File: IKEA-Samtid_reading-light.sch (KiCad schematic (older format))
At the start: 19 parts, among them P1 CONN_2, U1 PT4115-SOT89-5

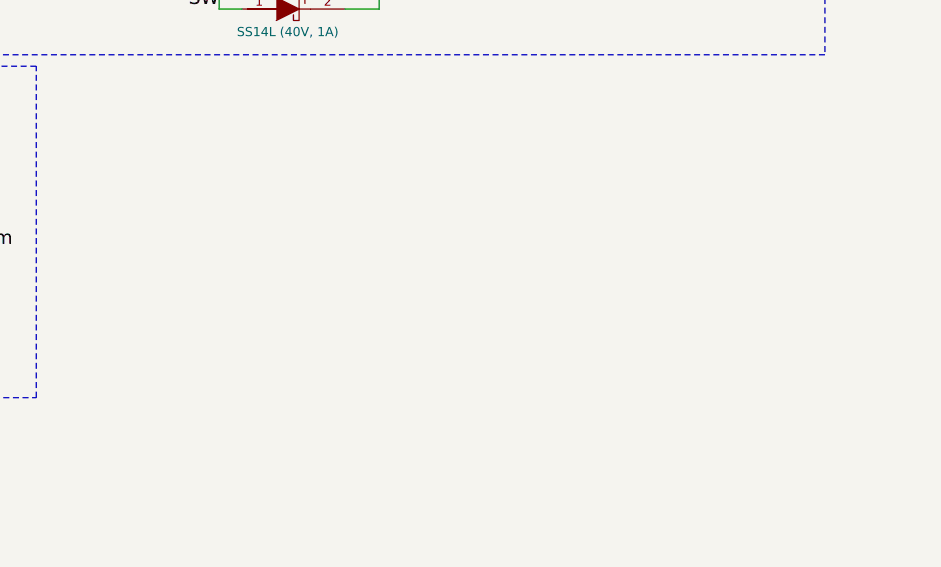
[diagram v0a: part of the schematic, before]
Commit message: Chose ATtiny25 for high-speed PWM (PLL).
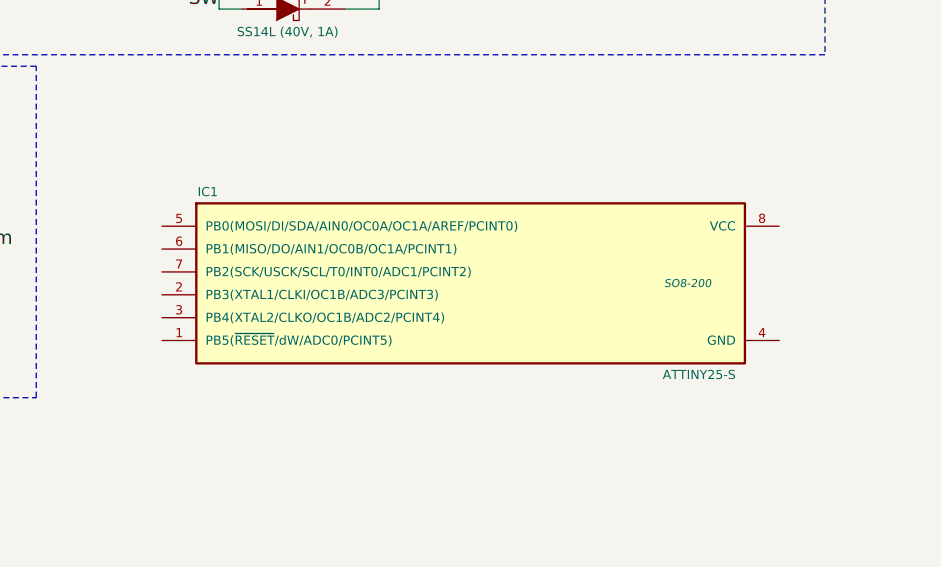
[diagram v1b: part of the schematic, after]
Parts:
- added IC1: ATTINY25-S, SO8-200, symbol ATTINY25-S
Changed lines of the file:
@@
 EESchema Schematic File Version 2
 LIBS:my_parts
+LIBS:atmel
 LIBS:power
 LIBS:device
@@
 LIBS:siliconi
 LIBS:opto
-LIBS:atmel
 LIBS:contrib
 LIBS:valves
@@
 Wire Wire Line
 	5900 2200 6000 2200
+$Comp
+L ATTINY25-S IC1
+U 1 1 5384DAB7
+P 3350 3100
+F 0 "IC1" H 2200 3500 40  0000 C CNN
+F 1 "ATTINY25-S" H 4350 2700 40  0000 C CNN
+F 2 "SO8-200" H 4300 3100 35  0000 C CIN
+F 3 "" H 3350 3100 60  0000 C CNN
+	1    3350 3100
+	1    0    0    -1
+$EndComp
 $EndSCHEMATC

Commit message: Shoving parts around.
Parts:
- removed C4: 10µF, symbol C
- removed P1: CONN_2, symbol CONN_2
- added C1: 10µF, symbol C
- added FSEN1, FSEN2: CONN_2, symbol CONN_2
- added JP1: AVR_ISP, symbol MADW__AVR_ISP
- added P1: CONN_4, symbol CONN_4
- added R_FS1, R_FS2: 1M, symbol R
- added U1: MCP1804-SOT23-5, symbol MADW__MCP1804-SOT23-5
- C2: value 10µF -> 100nF
- C4: renamed from C5; value 10µF -> 100nF
- C5: renamed from C1; value 10µF -> 100nF
- renumbered U1 to U2
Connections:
- net DIM: now also IC1.3 (PB4(XTAL2/CLKO/OC1B/ADC2/PCINT4))
- net GND: now also IC1.4 (GND), C1.2, FSEN2.2 (PM), JP1.6 (GND), P1.3 (P3), P1.4 (P4), R_FS2.2, U1.2 (GND)
- net RESET: now reaches IC1.1 (PB5(~RESET~/dW/ADC0/PCINT5))
- net RESET: now also JP1.5 (RST)
- net FSEN: now reaches IC1.2 (PB3(XTAL1/CLKI/OC1B/ADC3/PCINT3))
- net FSEN: now also FSEN1.2 (PM), FSEN2.1 (P1), R_FS1.2, R_FS2.1
- net MOSI: now reaches IC1.5 (PB0(MOSI/DI/SDA/AIN0/OC0A/OC1A/AREF/PCINT0))
- net MOSI: now also JP1.4 (MOSI)
- net MISO: now reaches IC1.6 (PB1(MISO/DO/AIN1/OC0B/OC1A/PCINT1))
- net MISO: now also JP1.1 (MISO)
- net SCK: now reaches IC1.7 (PB2(SCK/USCK/SCL/T0/INT0/ADC1/PCINT2))
- net SCK: now also JP1.3 (SCK)
- net +5V: now reaches IC1.8 (VCC)
- net +5V: now also C3.1, C4.1, FSEN1.1 (P1), JP1.2 (VTG), R_FS1.1, U1.5 (OUT)
- net D1HS: no longer names the net of D1.2 (K), D2.1 (A)
- net D2HS: no longer names the net of D2.2 (K), D3.1 (A)
- net D3HS: no longer names the net of D3.2 (K), D4.1 (A)
- net D4HS: no longer names the net of D4.2 (K), D5.1 (A)
- net D5HS: no longer names the net of D5.2 (K), D6.1 (A)
- net D6HS: no longer names the net of D6.2 (K), L1.2
- net VCC renamed +24V
- net +24V: now also C1.1, P1.1 (P1), P1.2 (P2), U1.1 (Vin), U1.4 (SHDN); no longer C3.1, C4.1
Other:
- note added: "5V power supply"
- note added: "Analog finger sensor"
- note added: "Brainz"
- note added: "LED driver + LEDs"
- note added: "PT4115 input protection"
- note removed: "(*) Don't use C6 when driving DIM with a 5V PWM signal.\n Replace R1 with a 10k pull-down resistor."
- note removed: "(24V)"
- moved on the sheet: C2, C4, C5, D1, D2, D3, D4, D5, D6, DS1, DZ1, IC1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

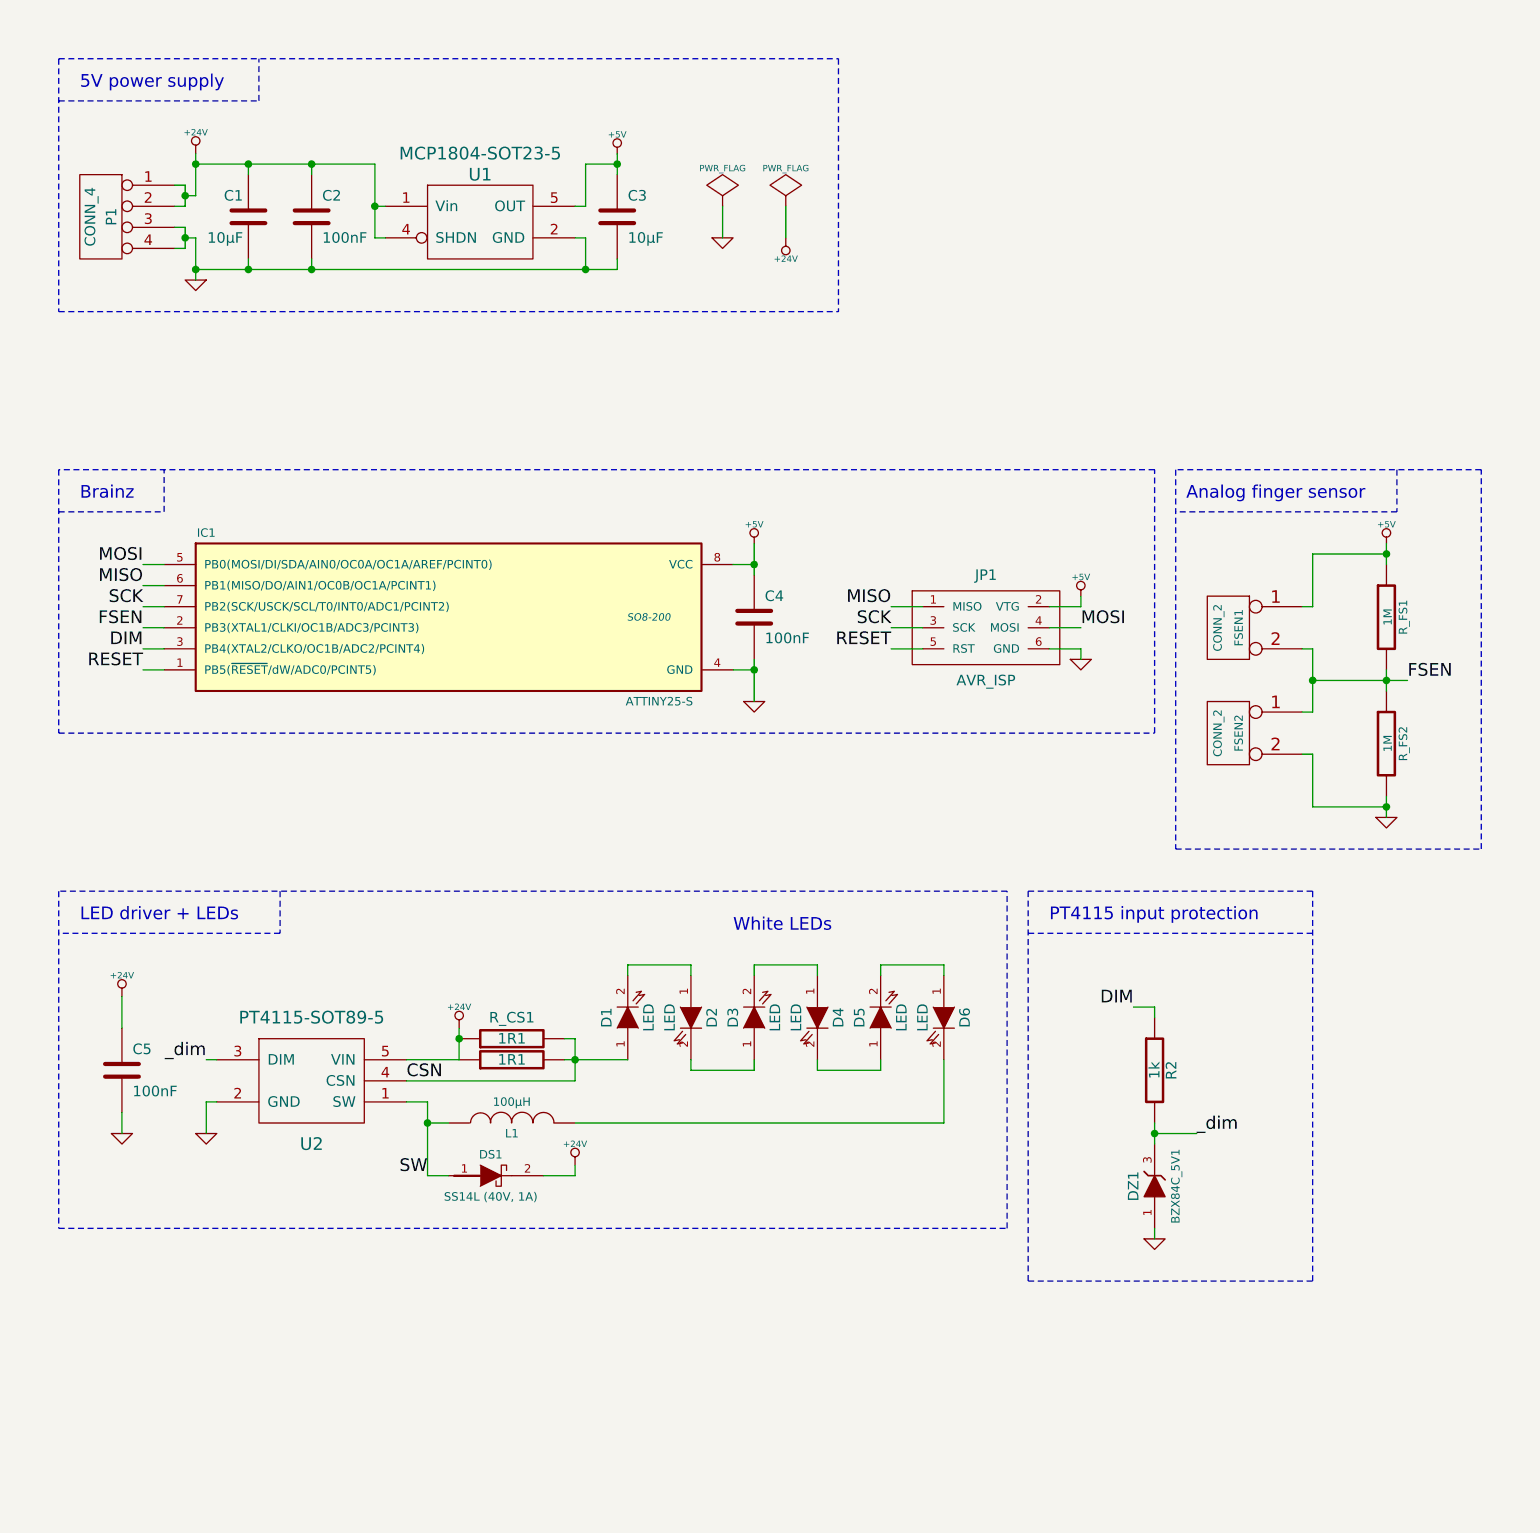
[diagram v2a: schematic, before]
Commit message: 1st fully routed board (quite chaotic).
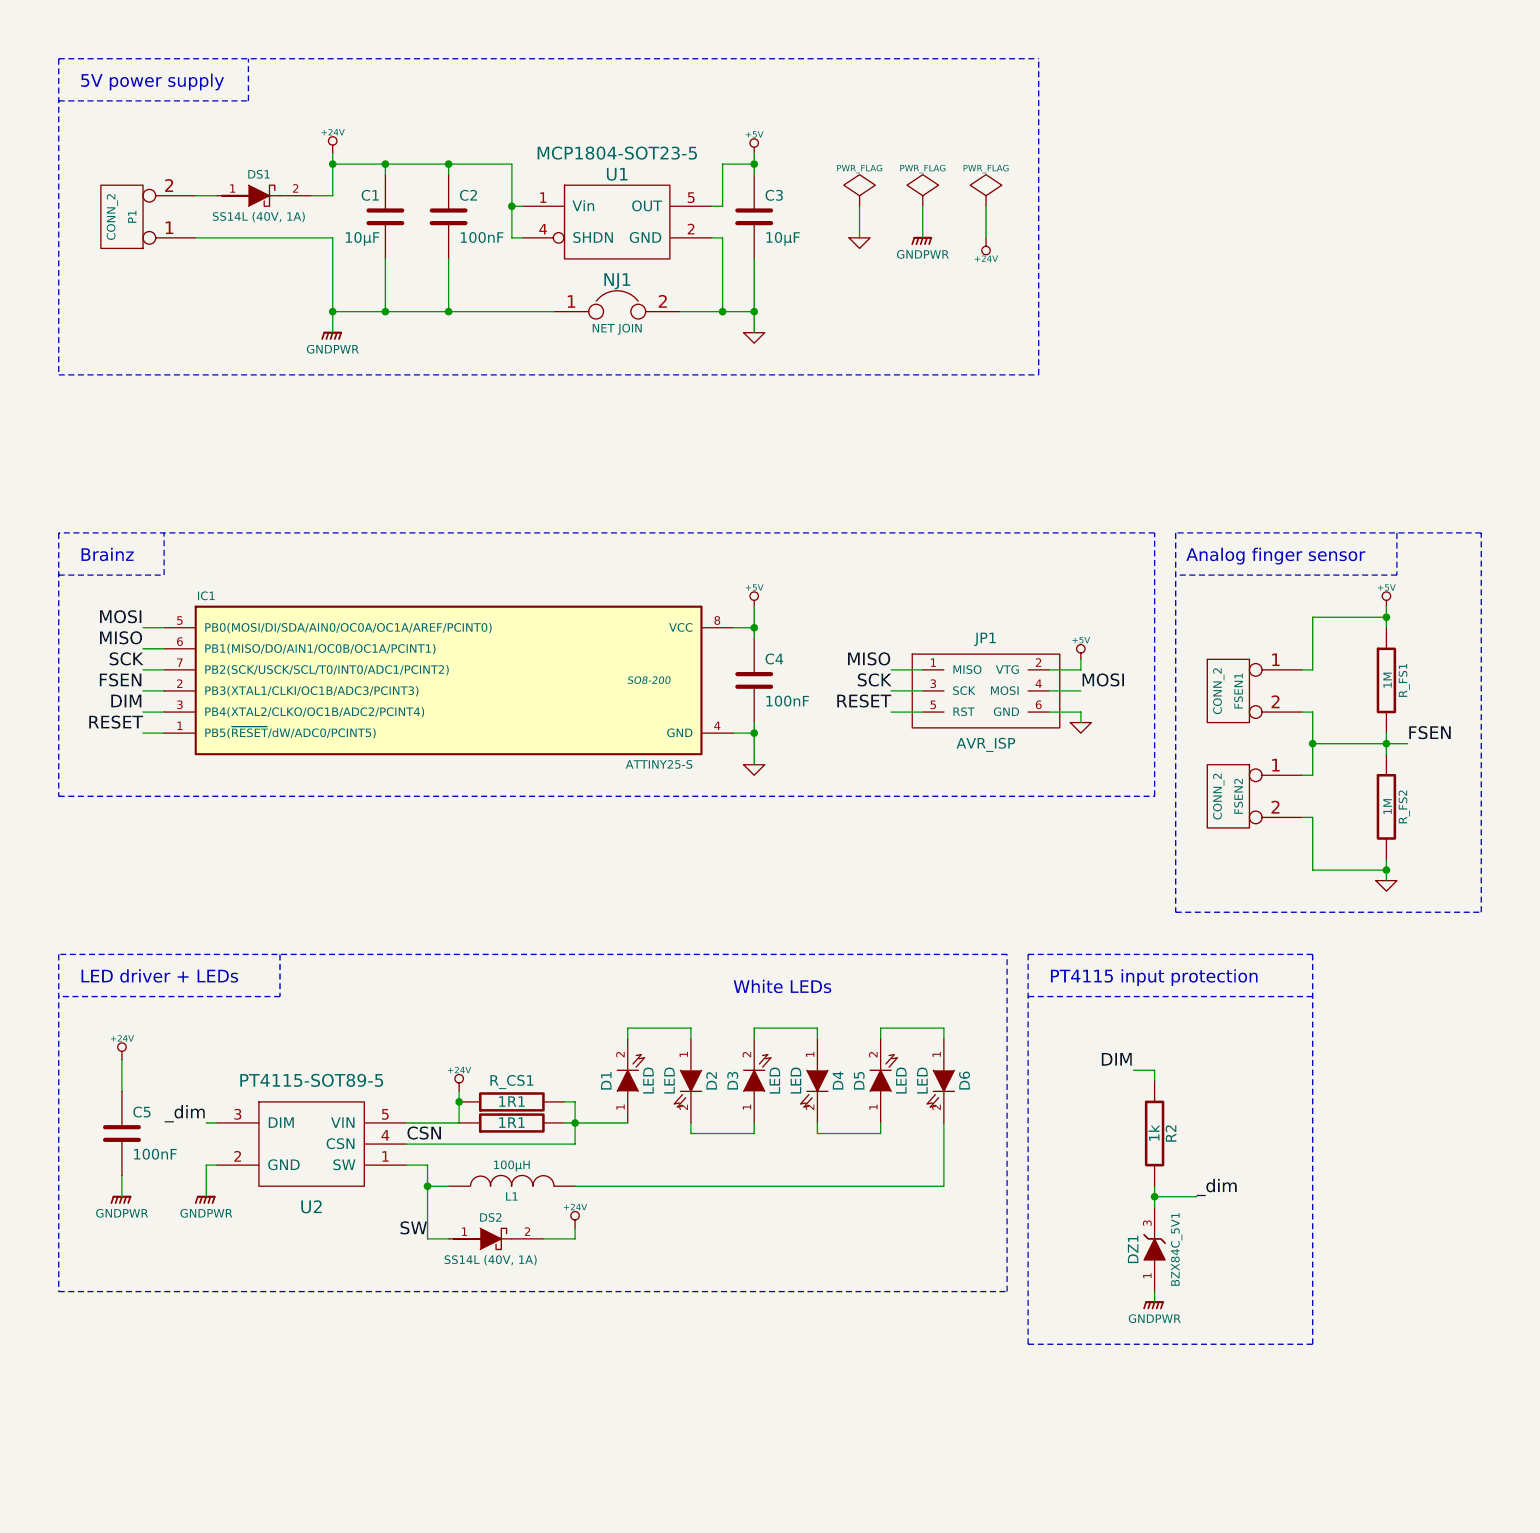
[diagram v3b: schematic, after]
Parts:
- removed P1: CONN_4, symbol CONN_4
- added DS1: SS14L (40V, 1A), symbol DIODESCH
- added NJ1: NET JOIN, symbol JUMPER
- added P1: CONN_2, symbol CONN_2
- renumbered DS1 to DS2
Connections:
- net +24V: now also DS1.2 (C)
- net GND: now also NJ1.2; no longer C1.2, C2.2, C5.2, DZ1.1, U2.2 (GND)
- new net: DS1.1 (A), P1.2 (PM)
- new net GNDPWR: C1.2, C2.2, C5.2, DZ1.1, NJ1.1, P1.1 (P1), U2.2 (GND)
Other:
- moved on the sheet: C1, C2, C3, C4, C5, D1, D2, D3, D4, D5, D6, DS2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

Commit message: R_FSx 1M --> 10M.
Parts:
- R_FS1, R_FS2: value 1M -> 10M
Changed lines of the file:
@@
 Sheet 1 1
 Title "IKEA-Samtid_reading-light"
-Date "27 May 2014"
+Date "29 May 2014"
 Rev "0.10"
 Comp "2014 - blog.spitzenpfeil.org"
@@
 P 7050 3700
 F 0 "R_FS1" V 7130 3700 40  0000 C CNN
-F 1 "1M" V 7057 3701 40  0000 C CNN
+F 1 "10M" V 7057 3701 40  0000 C CNN
 F 2 "" V 6980 3700 30  0000 C CNN
 F 3 "" H 7050 3700 30  0000 C CNN
@@
 P 7050 4300
 F 0 "R_FS2" V 7130 4300 40  0000 C CNN
-F 1 "1M" V 7057 4301 40  0000 C CNN
+F 1 "10M" V 7057 4301 40  0000 C CNN
 F 2 "" V 6980 4300 30  0000 C CNN
 F 3 "" H 7050 4300 30  0000 C CNN

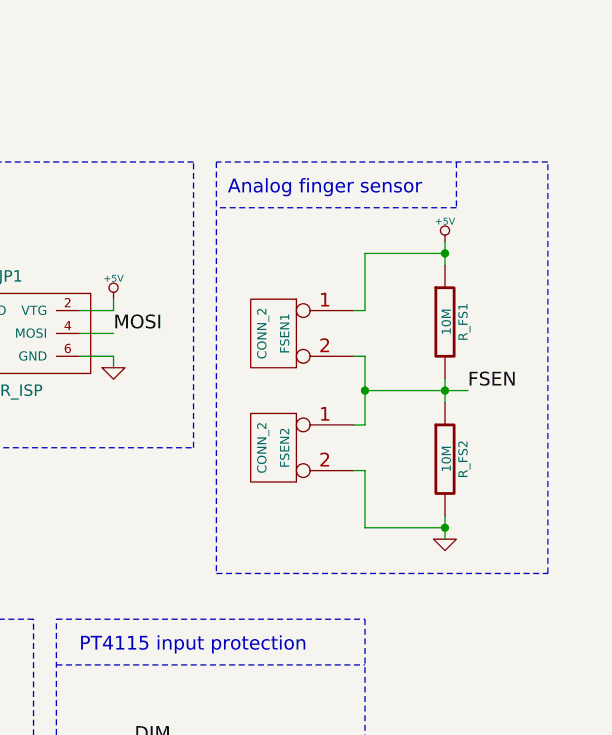
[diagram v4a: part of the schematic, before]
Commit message: Added a buffer-cap for the ADC input + minor layout tweaks.
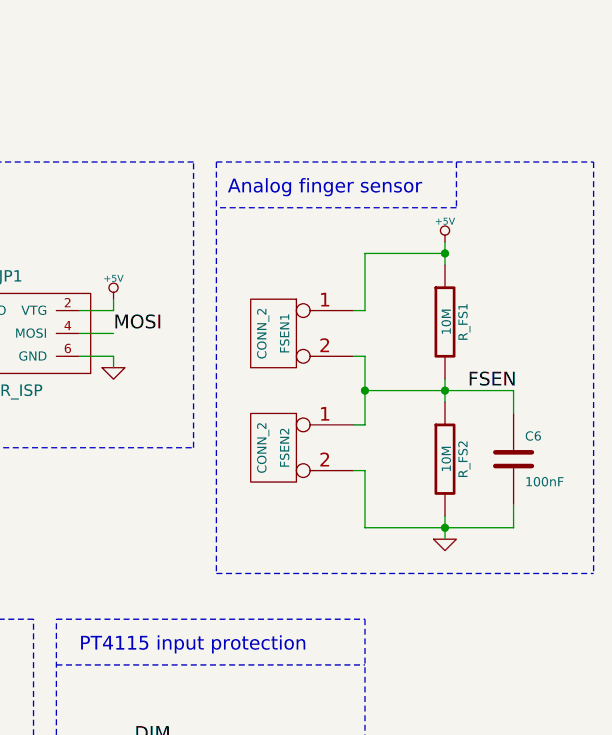
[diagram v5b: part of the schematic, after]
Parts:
- added C6: 100nF, symbol C
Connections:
- net FSEN: now also C6.1
- net GND: now also C6.2
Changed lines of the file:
@@
 	6700 3400 7050 3400
 Wire Wire Line
-	6700 4600 7050 4600
+	6700 4600 7350 4600
 Connection ~ 7050 4600
 Connection ~ 7050 3400
@@
 FSEN
 Wire Wire Line
-	6700 4000 7150 4000
-Wire Notes Line
-	6050 4800 7500 4800
+	6700 4000 7350 4000
+Wire Notes Line
+	6050 4800 7700 4800
 Text Notes 6100 3150 0    60   ~ 0
 Analog finger sensor
@@
 	6050 3000 6050 4800
 Wire Notes Line
-	7500 4800 7500 3000
-Wire Notes Line
 	7100 3200 6050 3200
 Wire Notes Line
 	7100 3000 7100 3200
 Wire Notes Line
-	7500 3000 6050 3000
+	6050 3000 7700 3000
 Wire Wire Line
 	2300 1700 2300 1950
@@
 Wire Notes Line
 	1650 950  1650 750
+$Comp
+L C C6
+U 1 1 538769C2
+P 7350 4300
+F 0 "C6" H 7400 4400 40  0000 L CNN
+F 1 "100nF" H 7400 4200 40  0000 L CNN
+F 2 "" H 7388 4150 30  0000 C CNN
+F 3 "" H 7350 4300 60  0000 C CNN
+	1    7350 4300
+	1    0    0    -1
+$EndComp
+Wire Wire Line
+	7350 4000 7350 4100
+Wire Wire Line
+	7350 4600 7350 4500
+Wire Notes Line
+	7700 3000 7700 4800
 $EndSCHEMATC
